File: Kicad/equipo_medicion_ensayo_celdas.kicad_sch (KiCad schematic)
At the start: 42 parts, among them J1 Micro_SD_Card, J2 Conn_Coaxial, J3 Conn_01x06, J4 USB_C_Receptacle_USB2.0_16P, SW1 SW_Push, SW2 SW_Push, U1 STM32WB55RGVx, U2 USBLC6-2SC6, U6 LM1117DT-3.3, X1 32.768kHz, X2 32MHz

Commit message: Avances en fuente partida del esquemático Kicad.
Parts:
- removed C1, C10, C15, C16, C2, C3, C4, C5, C6, C9: 100n, symbol Device:C
- removed C11, C12: C, symbol Device:C
- removed C13: 0p8, symbol Device:C
- removed C14: 0p3, symbol Device:C
- removed C36, C37: 10u, symbol Device:C
- removed C7, C8: 4u7, symbol Device:C
- removed D1: LED, symbol Device:LED
- removed D4, D5: B560C, symbol Device:D_Schottky
- removed FLT1: DLF162500LT-5028A1, equipo_medicion_ensayo_celdas_footprints:DLF162500LT-5028A1, symbol equipo_medicion_ensayo_celdas_sch_symbols:DLF162500LT-5028A1
- removed J1: Micro_SD_Card, symbol Connector:Micro_SD_Card
- removed J2: Conn_Coaxial, symbol Connector:Conn_Coaxial
- removed J3: Conn_01x06, Connector_PinHeader_2.54mm:PinHeader_1x06_P2.54mm_Vertical, symbol Connector_Generic:Conn_01x06
- removed J4: USB_C_Receptacle_USB2.0_16P, symbol Connector:USB_C_Receptacle_USB2.0_16P
- removed L1: 2n7, symbol Device:L
- removed R1, R3, R4: 5K1, symbol Device:R
- removed R18, R19, R20: 10k, symbol Device:R
- removed R2, R6: 220, symbol Device:R
- removed SW1, SW2: SW_Push, symbol Switch:SW_Push
- removed U1: STM32WB55RGVx, Package_DFN_QFN:QFN-68-1EP_8x8mm_P0.4mm_EP6.4x6.4mm, symbol MCU_ST_STM32WB:STM32WB55RGVx
- removed U2: USBLC6-2SC6, Package_TO_SOT_SMD:SOT-23-6, symbol Power_Protection:USBLC6-2SC6
- removed U6: LM1117DT-3.3, Package_TO_SOT_SMD:TO-252-3_TabPin2, symbol Regulator_Linear:LM1117DT-3.3
- removed X1: 32.768kHz, symbol Device:Crystal
- removed X2: 32MHz, symbol Device:Crystal_GND24_Small
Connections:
- no-connect marks 4 -> 0
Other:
- added sheet CELL_TESTER_MODULE (cell_tester_module.kicad_sch)
- added sheet SPLIT_POWER_SUPPLY (split_power_supply.kicad_sch)
- sheet CONTROL_AND_PROCESSING ports: added +5V_IN, ADC_IN1, ADC_IN10, ADC_IN11, ADC_IN12, ADC_IN13, ADC_IN14, ADC_IN15, ADC_IN16, ADC_IN2, ADC_IN3, ADC_IN4, ADC_IN5, ADC_IN6, ADC_IN7, ADC_IN8, ADC_IN9, MCP1_CS, MCP2_CS, MCP3_CS, MCP4_CS, SPI1_MOSI, SPI1_SCK; removed none

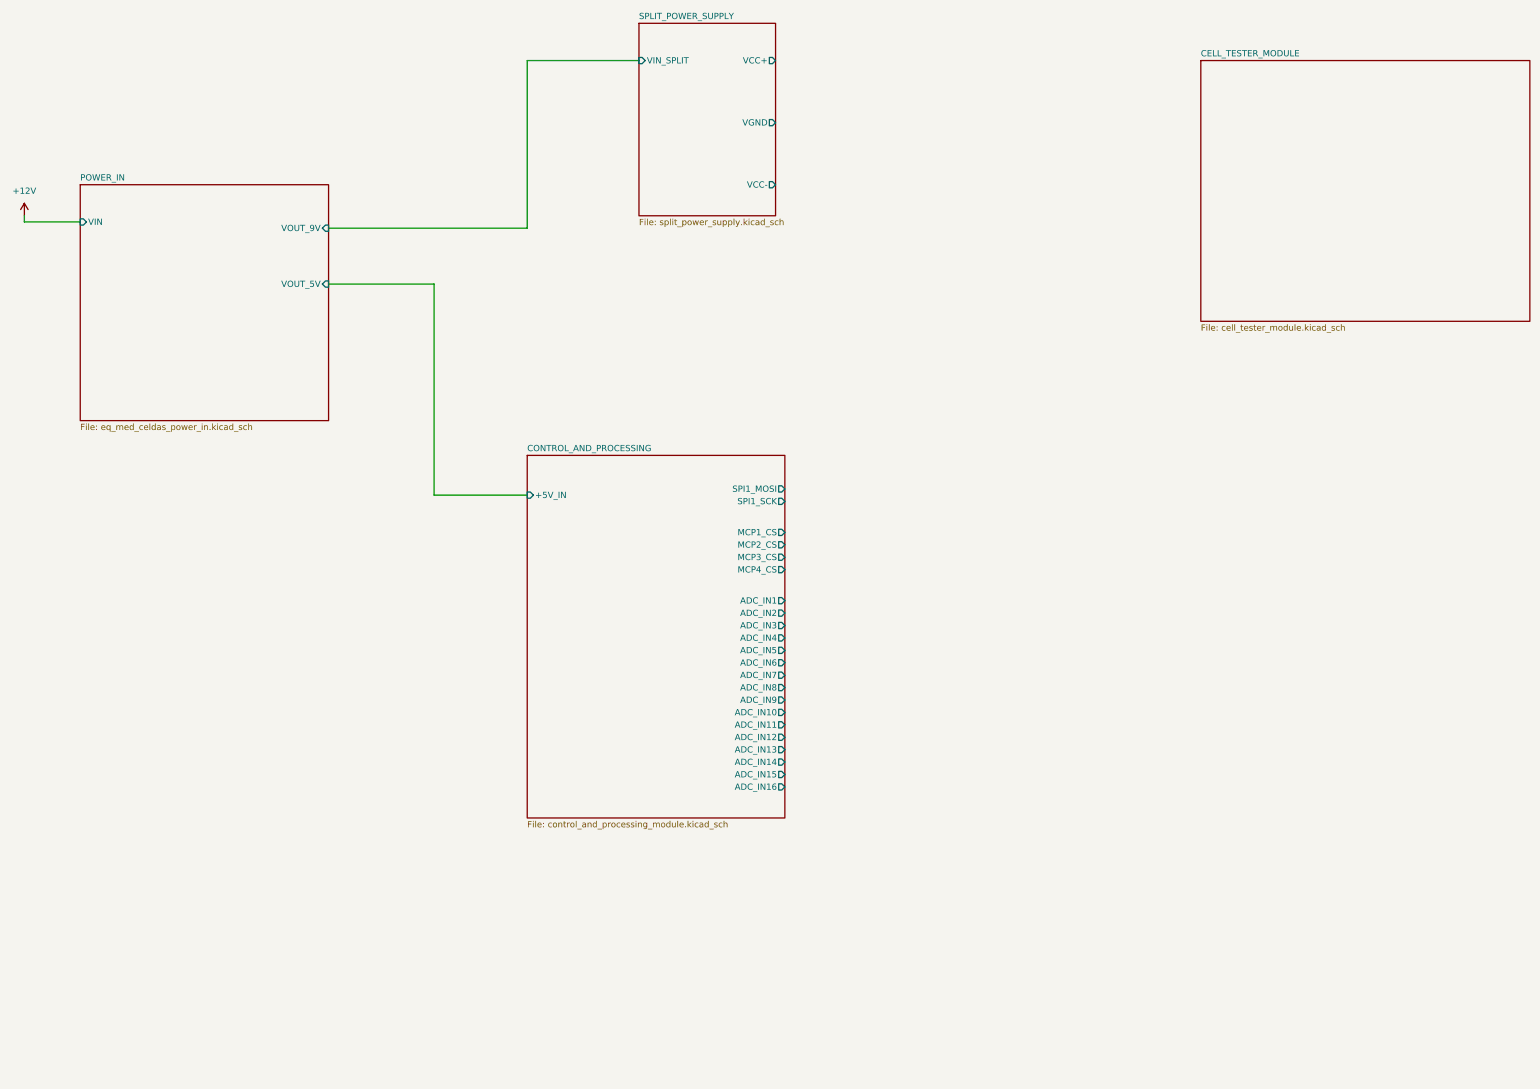
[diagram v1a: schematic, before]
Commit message: Pruebas y arreglos relacionados a compensación de lazo de tensión y mediciones de frontend de módulo de carga.
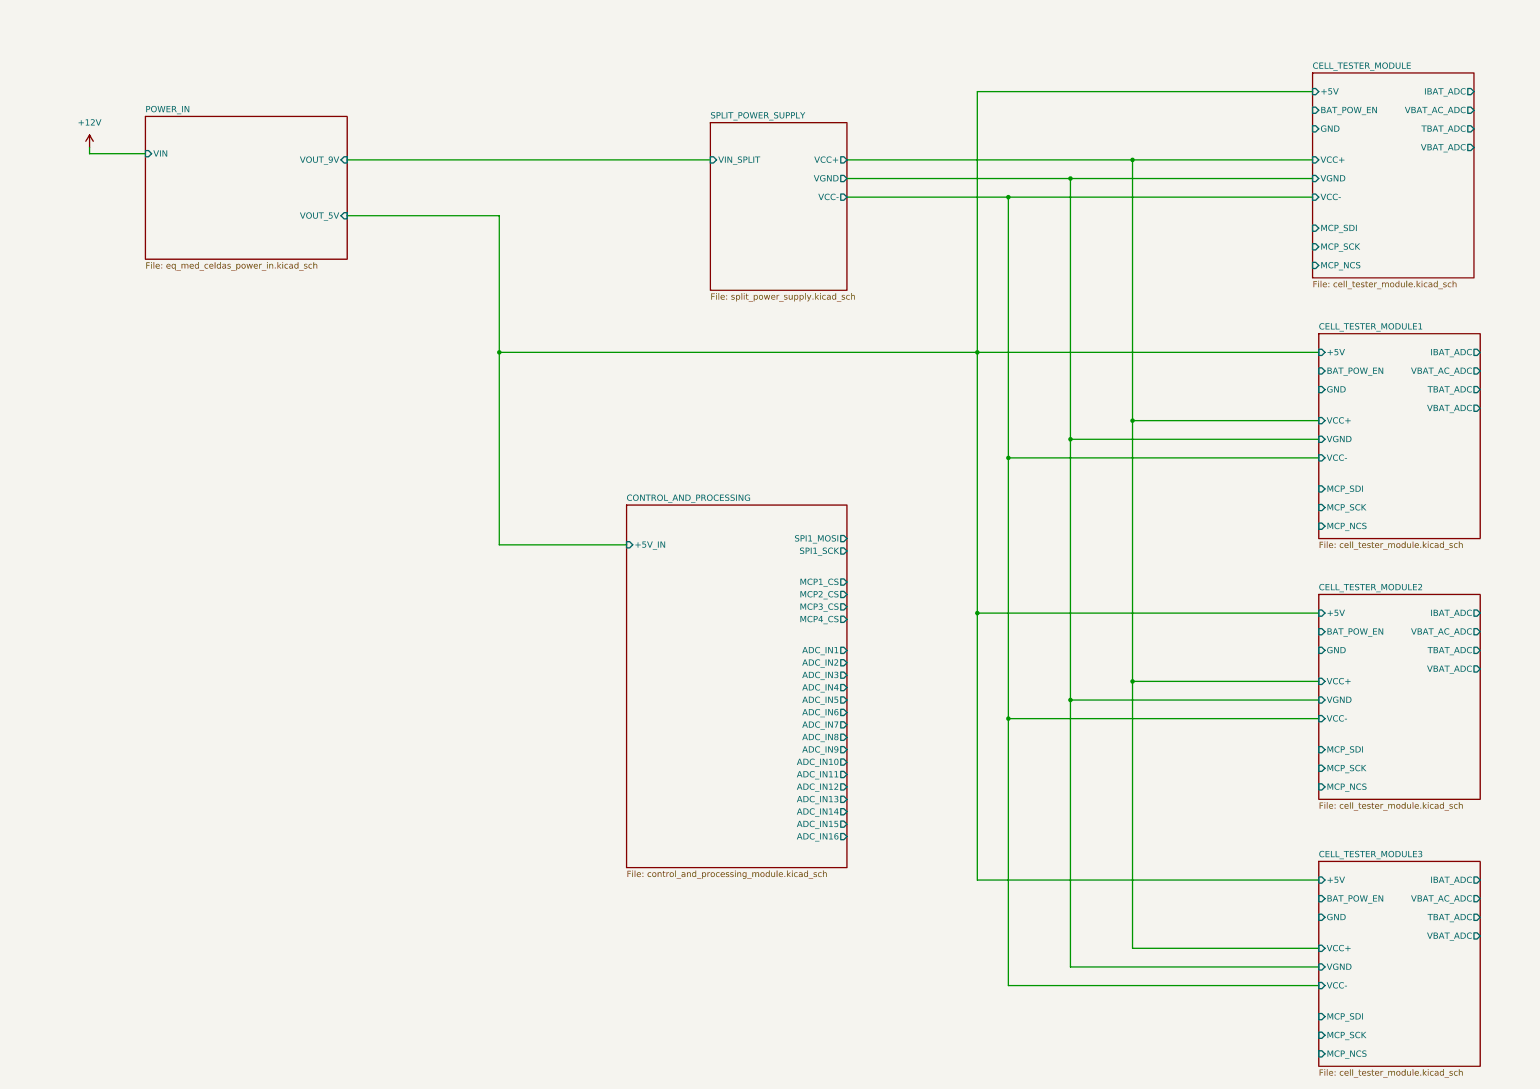
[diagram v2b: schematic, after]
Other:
- added sheet CELL_TESTER_MODULE1 (cell_tester_module.kicad_sch)
- added sheet CELL_TESTER_MODULE2 (cell_tester_module.kicad_sch)
- added sheet CELL_TESTER_MODULE3 (cell_tester_module.kicad_sch)
- sheet CELL_TESTER_MODULE ports: added +5V, BAT_POW_EN, GND, IBAT_ADC, MCP_NCS, MCP_SCK, MCP_SDI, TBAT_ADC, VBAT_AC_ADC, VBAT_ADC, VCC+, VCC-, VGND; removed none
- title: Placa prueba BQ24780s -> CELL TESTER EQ.

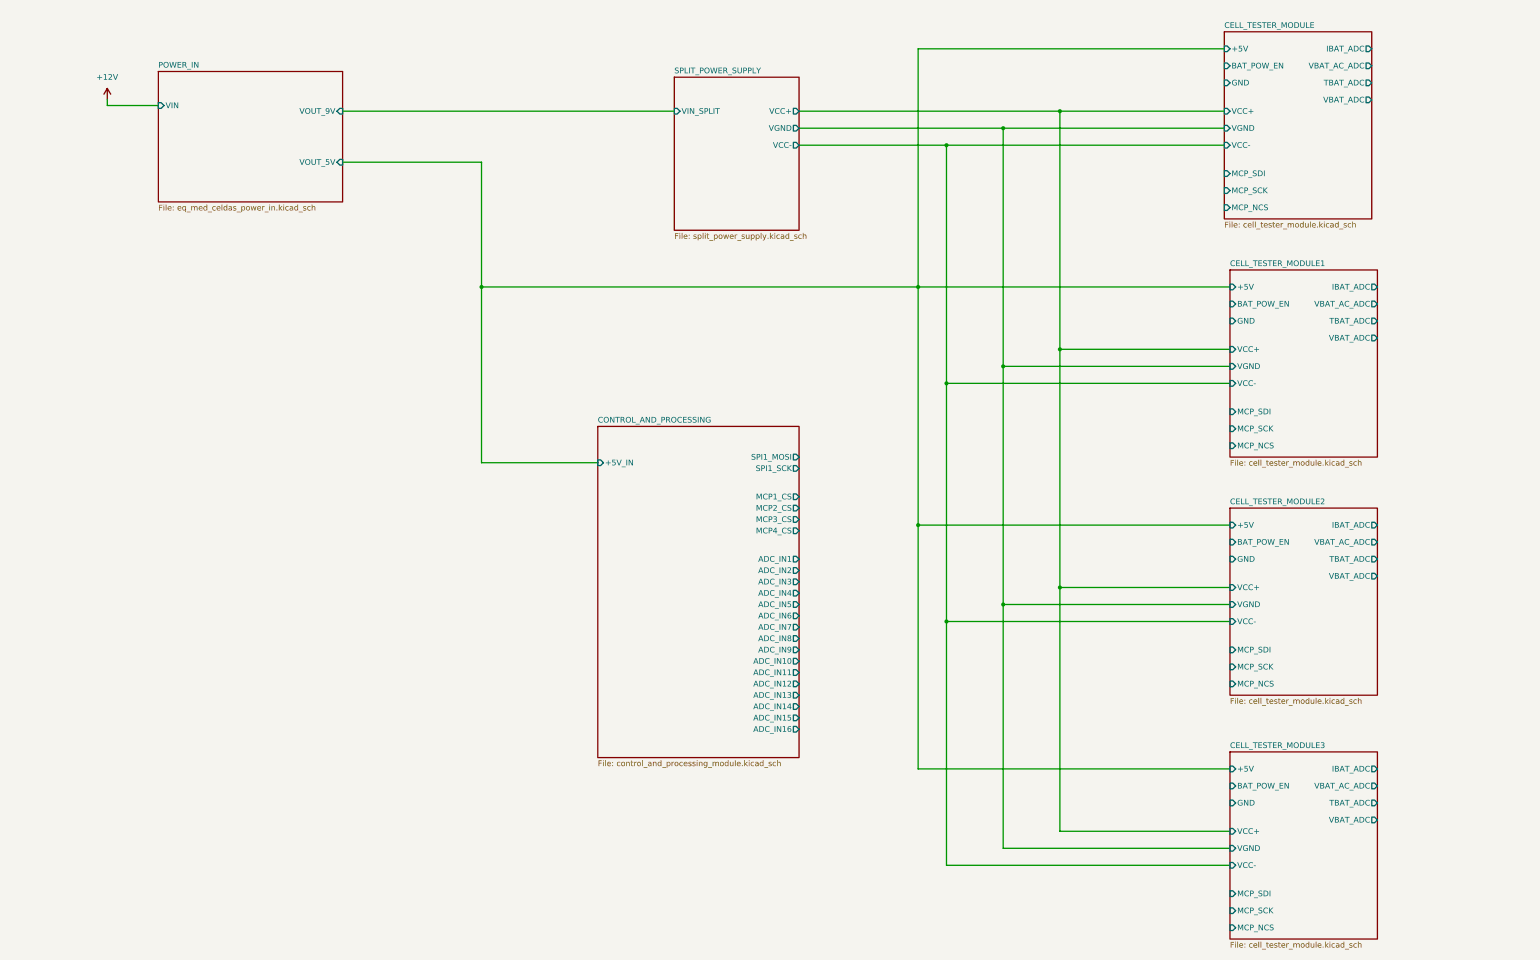
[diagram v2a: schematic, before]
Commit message: Correcciones y mejoras en esquemático y simulaciones.
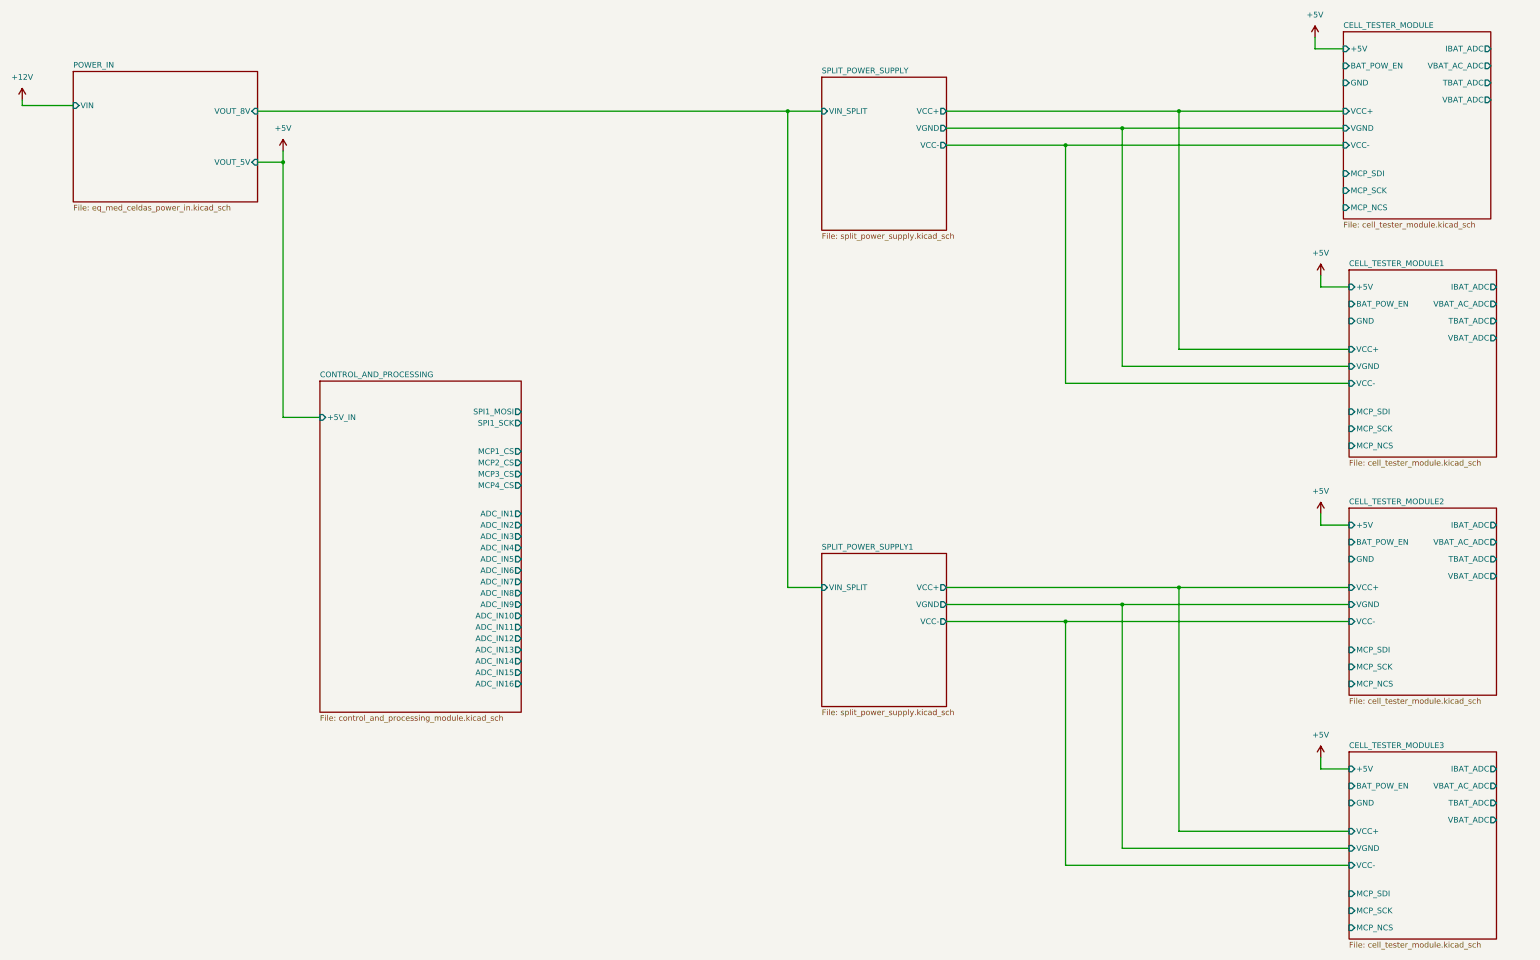
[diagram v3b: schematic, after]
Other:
- added sheet SPLIT_POWER_SUPPLY1 (split_power_supply.kicad_sch)
- sheet POWER_IN ports: added VOUT_8V; removed VOUT_9V

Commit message: Avances en el esquemático de Kicad.
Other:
- added sheet DACS_MODULE (dacs_module.kicad_sch)
- sheet CELL_TESTER_MODULE ports: added I_CTRL, V_CTRL; removed MCP_NCS, MCP_SCK, MCP_SDI
- sheet CELL_TESTER_MODULE1 ports: added I_CTRL, V_CTRL; removed MCP_NCS, MCP_SCK, MCP_SDI
- sheet CELL_TESTER_MODULE2 ports: added I_CTRL, V_CTRL; removed MCP_NCS, MCP_SCK, MCP_SDI
- sheet CELL_TESTER_MODULE3 ports: added I_CTRL, V_CTRL; removed MCP_NCS, MCP_SCK, MCP_SDI
